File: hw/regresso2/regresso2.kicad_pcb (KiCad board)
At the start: 2 copper layers, 53.9 x 53.3 mm, 34 parts, among them J1 CONN_01X02, J2 Conn_01x08, J3 Conn_01x06, J4 Conn_01x10, J5 Conn_01x08, P10 CONTROL, P11 CONN_01X06, P9 FX2LA, U1 STM32L151C6TxA, U2 MIC550x-3.3YM5, Y1 Crystal_GND24_Small

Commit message: h2/regresso2: nearly "finished"
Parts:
- moved PB10 38.8 mm to (126.7, 105.4)
- moved PB11 38.8 mm to (126.7, 102.1)
- moved PB0 34.4 mm to (132.8, 114.4)
- moved PB1 32.7 mm to (134.0, 111.1)
- moved PA1 32.3 mm to (126.4, 110.4)
- moved PA0 31.2 mm to (128.0, 114.2)
- moved R1 22.9 mm to (135.6, 84.5), turned to 90 degrees
- moved JP1 18.9 mm to (133.1, 81.3), turned to 0 degrees
- moved R2 16.3 mm to (132.5, 86.2), turned to 180 degrees
- moved JP2 13.2 mm to (130.6, 81.3), turned to 0 degrees
- moved P11 2.84 mm to (152.3, 120.0)
- moved C4 1.39 mm to (145.0, 95.6)
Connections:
- J2 pad 1: (no net) -> Net-(J2-Pad1)
- J2 pad 2: (no net) -> Net-(J2-Pad2)
- J2 pad 3: (no net) -> Net-(J2-Pad3)
- J2 pad 4: (no net) -> Net-(J2-Pad4)
- J2 pad 5: (no net) -> Net-(J2-Pad5)
- J2 pad 8: (no net) -> Net-(J2-Pad8)
- J3 pad 4: (no net) -> Net-(J3-Pad4)
- J3 pad 5: (no net) -> Net-(J3-Pad5)
- J3 pad 6: (no net) -> Net-(J3-Pad6)
- J4 pad 2: (no net) -> Net-(J4-Pad2)
- J4 pad 3: (no net) -> Net-(J4-Pad3)
- J4 pad 8: (no net) -> Net-(J4-Pad8)
- J5 pad 1: (no net) -> Net-(J5-Pad1)
- J5 pad 2: (no net) -> Net-(J5-Pad2)
- J5 pad 4: (no net) -> Net-(J5-Pad4)
- J5 pad 5: (no net) -> Net-(J5-Pad5)
- J5 pad 6: (no net) -> Net-(J5-Pad6)
- J5 pad 7: (no net) -> Net-(J5-Pad7)
- J5 pad 8: (no net) -> /USART_CK_OUT
- P10 pad 4: (no net) -> Net-(P10-Pad4)
- P9 pad 3: /UART_TX_OUT -> /SPI_MOSI
- P9 pad 4: /UART_RX_OUT -> /SPI_MISO
- P9 pad 5: /SPI_MOSI -> /SPI_SCK
- P9 pad 6: /SPI_MISO -> /SPI_CS
- P9 pad 7: /SPI_SCK -> /UART_TX_OUT
- P9 pad 8: /SPI_CS -> /UART_RX_OUT
- P9 pad 9: (no net) -> Net-(P9-Pad9)
- R3 pad 1: (no net) -> /LED_CONTROL
- U1 pad 10: Net-(PA0-Pad1) -> Net-(U1-Pad10)
- U1 pad 11: Net-(PA1-Pad1) -> Net-(U1-Pad11)
- U1 pad 12: (no net) -> Net-(U1-Pad12)
- U1 pad 13: (no net) -> Net-(U1-Pad13)
- U1 pad 16: (no net) -> Net-(U1-Pad16)
- U1 pad 17: (no net) -> Net-(U1-Pad17)
- U1 pad 18: Net-(PB0-Pad1) -> Net-(U1-Pad18)
- U1 pad 19: Net-(PB1-Pad1) -> Net-(U1-Pad19)
- U1 pad 2: (no net) -> Net-(U1-Pad2)
- U1 pad 20: (no net) -> Net-(U1-Pad20)
- U1 pad 21: Net-(PB10-Pad1) -> Net-(U1-Pad21)
- U1 pad 22: Net-(PB11-Pad1) -> Net-(U1-Pad22)
- U1 pad 29: (no net) -> /UART_CK_OUT
- U1 pad 3: (no net) -> Net-(U1-Pad3)
- U1 pad 38: (no net) -> Net-(U1-Pad38)
- U1 pad 4: (no net) -> Net-(U1-Pad4)
- U1 pad 40: (no net) -> Net-(U1-Pad40)
- U1 pad 41: (no net) -> Net-(U1-Pad41)
- U1 pad 42: (no net) -> Net-(U1-Pad42)
- U1 pad 43: (no net) -> Net-(U1-Pad43)
- U2 pad 4: (no net) -> Net-(U2-Pad4)
- Y1 pad 2: (no net) -> Net-(Y1-Pad2)
- Y1 pad 4: (no net) -> Net-(Y1-Pad4)
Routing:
- net /SWDIO: track 8.93 -> 57.1 mm
- net +3V3: track 133.6 -> 88.8 mm, vias 6 -> 5
- net /UART_RX_OUT: track 32.7 -> 74.9 mm, vias 2 -> 0
- net /I2C_SDA: track 29.7 -> 61.8 mm
- net /SWCLK: track 11.1 -> 42.1 mm
- net Net-(U1-Pad16): track 28.2 -> 0.00 mm
- net /I2C_SCL: track 41.8 -> 67.4 mm
- net /SPI_CS: track 36.8 -> 57.2 mm, vias 1 -> 0
- net /SWO: track 9.32 -> 28.5 mm
- net /UART_TX_OUT: track 32.2 -> 50.6 mm, vias 2 -> 1
- net /NRST: track 9.68 -> 27.1 mm
- net Net-(PB11-Pad1): track 15.4 -> 0.00 mm
- net Net-(PB10-Pad1): track 12.8 -> 0.00 mm
- net Net-(PB1-Pad1): track 9.44 -> 0.00 mm
- net Net-(PA0-Pad1): track 8.31 -> 0.00 mm
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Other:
- board text removed: "ADC1-IN"

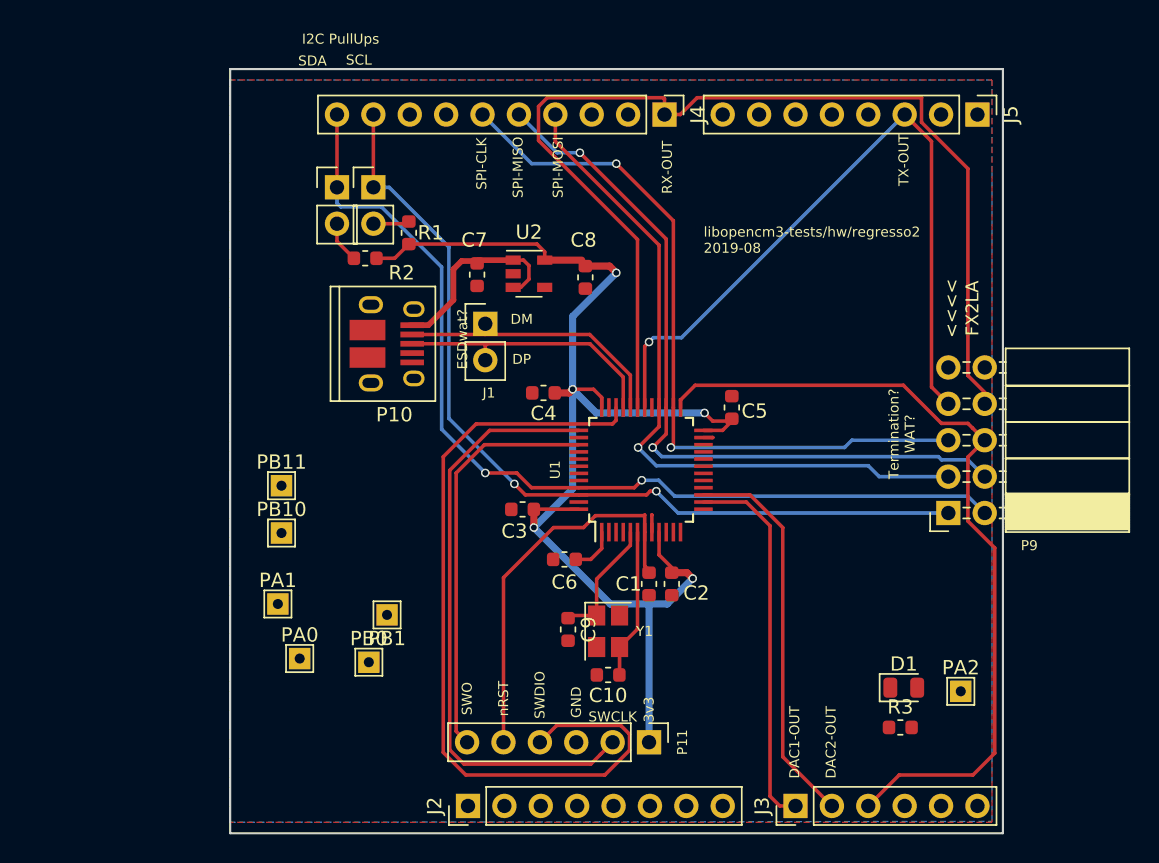
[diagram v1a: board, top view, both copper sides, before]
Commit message: hw/regresso2: "finished"
just need to start hacking at the board outline to fit around the nucleo
again.
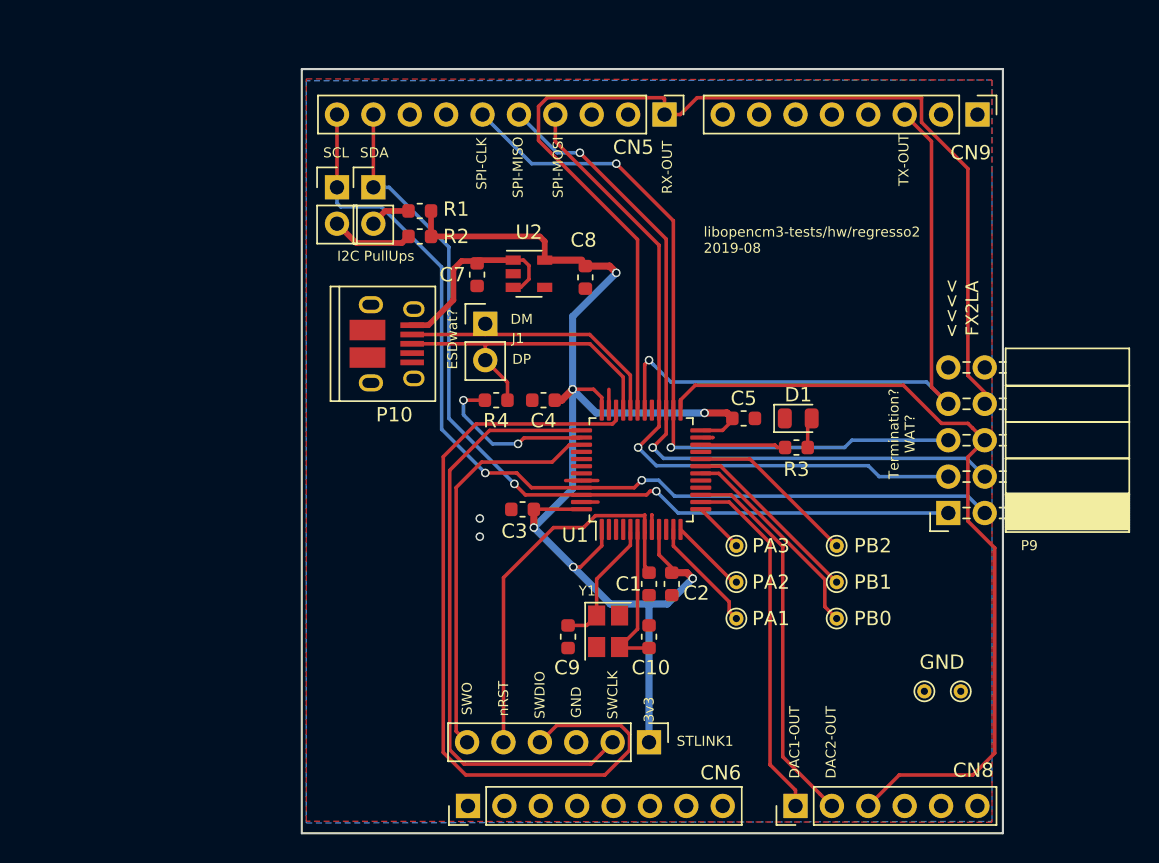
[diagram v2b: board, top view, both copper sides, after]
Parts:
- removed C6: 100n, Capacitor_SMD:C_0603_1608Metric
- removed PB11: TEST_1P, TestPoint:TestPoint_THTPad_1.5x1.5mm_Drill0.7mm
- added GND2: TEST_1P, TestPoint:TestPoint_THTPad_D1.0mm_Drill0.5mm, F.Cu at (171.6, 116.5)
- added PA1: TEST_1P, TestPoint:TestPoint_THTPad_D1.0mm_Drill0.5mm, F.Cu at (158.4, 111.4)
- added R4: 1,5k, Resistor_SMD:R_0603_1608Metric, F.Cu at (141.7, 96.1)
- GND1: renamed from PA2; footprint TestPoint:TestPoint_THTPad_1.5x1.5mm_Drill0.7mm -> TestPoint:TestPoint_THTPad_D1.0mm_Drill0.5mm
- PA2: renamed from PA0; footprint TestPoint:TestPoint_THTPad_1.5x1.5mm_Drill0.7mm -> TestPoint:TestPoint_THTPad_D1.0mm_Drill0.5mm
- PA3: renamed from PA1; footprint TestPoint:TestPoint_THTPad_1.5x1.5mm_Drill0.7mm -> TestPoint:TestPoint_THTPad_D1.0mm_Drill0.5mm
- PB0, PB1: footprint TestPoint:TestPoint_THTPad_1.5x1.5mm_Drill0.7mm -> TestPoint:TestPoint_THTPad_D1.0mm_Drill0.5mm
- PB2: renamed from PB10; footprint TestPoint:TestPoint_THTPad_1.5x1.5mm_Drill0.7mm -> TestPoint:TestPoint_THTPad_D1.0mm_Drill0.5mm
- STLINK1: renamed from P11; value CONN_01X06 -> STLINK
- U1: value STM32L151C6TxA -> STM32F303CCTx; footprint Housings_QFP:TQFP-48_7x7mm_Pitch0.5mm -> Package_QFP:LQFP-48_7x7mm_P0.5mm
- moved PB2 38.8 mm to (165.4, 106.3)
- moved PB0 32.8 mm to (165.4, 111.4)
- moved PA3 32.3 mm to (158.4, 106.3)
- moved PB1 31.5 mm to (165.4, 108.8)
- moved PA2 30.9 mm to (158.4, 108.8)
- moved R3 20.8 mm to (162.6, 99.4)
- moved D1 20.2 mm to (162.8, 97.4)
- moved R2 4.10 mm to (136.3, 84.7)
- moved C10 3.91 mm to (152.3, 112.6), turned to 90 degrees
- moved R1 1.70 mm to (136.3, 82.9), turned to 180 degrees
- moved C5 1.12 mm to (158.9, 97.4), turned to 0 degrees
- moved C4 0.51 mm to (145.0, 96.1)
- moved C9 0.51 mm to (146.7, 112.6)
- renumbered J4 to CN5, J2 to CN6, J3 to CN8, J5 to CN9
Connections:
- CN5 pad 2: Net-(J4-Pad2) -> (no net)
- CN5 pad 3: Net-(J4-Pad3) -> (no net)
- CN5 pad 8: Net-(J4-Pad8) -> (no net)
- CN6 pad 1: Net-(J2-Pad1) -> (no net)
- CN6 pad 2: Net-(J2-Pad2) -> (no net)
- CN6 pad 3: Net-(J2-Pad3) -> (no net)
- CN6 pad 4: Net-(J2-Pad4) -> (no net)
- CN6 pad 5: Net-(J2-Pad5) -> (no net)
- CN6 pad 8: Net-(J2-Pad8) -> (no net)
- CN8 pad 4: Net-(J3-Pad4) -> (no net)
- CN8 pad 5: Net-(J3-Pad5) -> (no net)
- CN8 pad 6: Net-(J3-Pad6) -> (no net)
- CN9 pad 1: Net-(J5-Pad1) -> (no net)
- CN9 pad 2: Net-(J5-Pad2) -> (no net)
- CN9 pad 4: Net-(J5-Pad4) -> (no net)
- CN9 pad 5: Net-(J5-Pad5) -> (no net)
- CN9 pad 6: Net-(J5-Pad6) -> (no net)
- CN9 pad 7: Net-(J5-Pad7) -> (no net)
- CN9 pad 8: /USART_CK_OUT -> (no net)
- P10 pad 4: Net-(P10-Pad4) -> (no net)
- P9 pad 9: Net-(P9-Pad9) -> (no net)
- PB2 pad 1: Net-(PB10-Pad1) -> Net-(PB2-Pad1)
- R3 pad 1: /LED_CONTROL -> /LED
- U1 pad 1: /VLCD -> +3V3
- U1 pad 10: Net-(U1-Pad10) -> (no net)
- U1 pad 12: Net-(U1-Pad12) -> Net-(PA0-Pad1)
- U1 pad 13: Net-(U1-Pad13) -> Net-(PA1-Pad1)
- U1 pad 16: Net-(U1-Pad16) -> (no net)
- U1 pad 17: Net-(U1-Pad17) -> (no net)
- U1 pad 18: Net-(U1-Pad18) -> Net-(PB0-Pad1)
- U1 pad 19: Net-(U1-Pad19) -> Net-(PB1-Pad1)
- U1 pad 2: Net-(U1-Pad2) -> (no net)
- U1 pad 20: Net-(U1-Pad20) -> Net-(PB2-Pad1)
- U1 pad 21: Net-(U1-Pad21) -> (no net)
- U1 pad 22: Net-(U1-Pad22) -> /LED
- U1 pad 29: /UART_CK_OUT -> (no net)
- U1 pad 3: Net-(U1-Pad3) -> (no net)
- U1 pad 4: Net-(U1-Pad4) -> (no net)
- U1 pad 40: Net-(U1-Pad40) -> (no net)
- U1 pad 41: Net-(U1-Pad41) -> (no net)
- U1 pad 42: Net-(U1-Pad42) -> (no net)
- U1 pad 43: Net-(U1-Pad43) -> (no net)
- U2 pad 4: Net-(U2-Pad4) -> (no net)
- Y1 pad 2: Net-(Y1-Pad2) -> (no net)
- Y1 pad 4: Net-(Y1-Pad4) -> (no net)
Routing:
- net Net-(PB0-Pad1): track 0.00 -> 14.8 mm
- net Net-(PB1-Pad1): track 0.00 -> 12.8 mm
- net Net-(PB2-Pad1): track 0.00 -> 12.0 mm
- net Net-(R4-Pad2): track 0.00 -> 11.8 mm, vias 0 -> 2
- net Net-(PB11-Pad1): track 0.00 -> 8.04 mm
- net /LED: track 0.00 -> 5.97 mm
- net Net-(PA0-Pad1): track 0.00 -> 5.42 mm
- net GND: track 1.87 -> 6.72 mm, vias 0 -> 2
- net Net-(PA1-Pad1): track 0.00 -> 3.58 mm
- net /UART_TX_OUT: track 50.6 -> 47.0 mm
- net /USB_DP: track 19.0 -> 22.4 mm
- net /VLCD: track 3.11 -> 0.00 mm
- net Net-(JP2-Pad2): track 2.90 -> 5.74 mm
- net Net-(D1-Pad2): track 0.00 -> 2.15 mm
- net +3V3: track 88.8 -> 90.9 mm, vias 5 -> 6
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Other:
- board size 53.9 x 53.3 mm -> 48.9 x 53.3 mm

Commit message: regresso2: board fixed
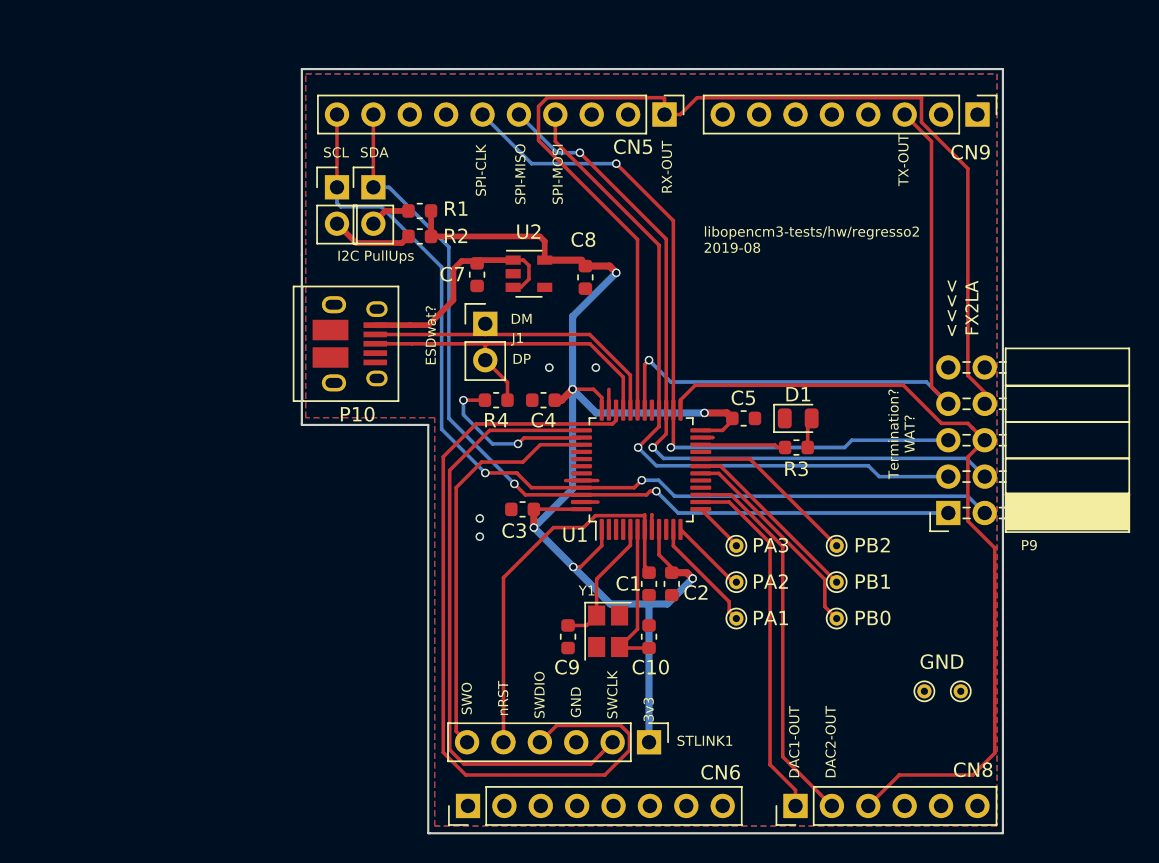
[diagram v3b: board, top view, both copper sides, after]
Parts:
- moved P10 2.58 mm to (131.7, 92.2)
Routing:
- net /USB_DM: track 18.7 -> 22.0 mm
- net /USB_DP: track 22.4 -> 25.0 mm
- net +5V: track 14.1 -> 16.5 mm
- net GND: vias 2 -> 4
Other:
- outline, holes or cut-outs redrawn
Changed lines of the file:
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@@
   (general
     (thickness 1.6)
-    (drawings 27)
-    (tracks 275)
+    (drawings 33)
+    (tracks 282)
     (modules 35)
     (nets 34)
@@
     (aux_axis_origin 123.1265 126.365)
     (grid_origin 123.1265 126.365)
-    (visible_elements FFFEFFFF)
+    (visible_elements FFFEF7FF)
     (pcbplotparams
       (layerselection 0x010f0_80000001)
@@
   )
   (module "Connectors:USB_Micro-B_10103594-0001LF" (layer "F.Cu")
-    (at 134.3025 92.202 270)
+    (at 131.7265 92.202 270)
     (descr "Micro USB Type B 10103594-0001LF")
     (tags "USB USB_B USB_micro USB_OTG")
@@
       (net 13 "Net-(P10-Pad6)"))
   )
+  (gr_line (start 128.1 97.765) (end 128.1 97.865) (layer "Edge.Cuts") (width 0.15))
+  (gr_line (start 130.7265 97.865) (end 128.1 97.865) (layer "Edge.Cuts") (width 0.15))
+  (gr_line (start 128.1 86) (end 128.1 97.765) (layer "Edge.Cuts") (width 0.15))
+  (gr_line (start 136.9265 126.365) (end 137.0457 126.365) (layer "Edge.Cuts") (width 0.15))
+  (gr_line (start 136.9265 97.865) (end 136.9265 126.365) (layer "Edge.Cuts") (width 0.15))
+  (gr_line (start 130.7265 97.865) (end 136.9265 97.865) (layer "Edge.Cuts") (width 0.15))
+  (gr_line (start 137.0457 126.365) (end 177.038 126.365) (angle 90) (layer "Edge.Cuts") (width 0.15))
   (gr_text "GND" (at 172.7835 114.427) (layer "F.SilkS")
     (effects (font (size 1 1) (thickness 0.15)))
@@
     (effects (font (size 0.7 0.7) (thickness 0.12)))
   )
-  (gr_text "SPI-CLK" (at 140.6525 79.629 90) (layer "F.SilkS")
+  (gr_text "SPI-CLK" (at 140.6265 80.115 90) (layer "F.SilkS")
     (effects (font (size 0.7 0.7) (thickness 0.12)))
   )
-  (gr_text "SPI-MISO" (at 143.1925 79.883 90) (layer "F.SilkS")
+  (gr_text "SPI-MISO" (at 143.3765 80.365 90) (layer "F.SilkS")
     (effects (font (size 0.7 0.7) (thickness 0.12)))
   )
-  (gr_text "SPI-MOSI" (at 145.9865 79.883 90) (layer "F.SilkS")
+  (gr_text "SPI-MOSI" (at 145.9865 80.365 90) (layer "F.SilkS")
     (effects (font (size 0.7 0.7) (thickness 0.12)))
   )
@@
     (effects (font (size 0.7 0.7) (thickness 0.12)))
   )
-  (gr_text "ESDwat?" (at 138.6205 91.8845 90) (layer "F.SilkS")
+  (gr_text "ESDwat?" (at 137.1265 91.615 90) (layer "F.SilkS")
     (effects (font (size 0.7 0.7) (thickness 0.12)))
   )
   (gr_line (start 177.038 126.365) (end 177.038 73.025) (angle 90) (layer "Edge.Cuts") (width 0.15))
-  (gr_line (start 128.1 126.365) (end 177.038 126.365) (angle 90) (layer "Edge.Cuts") (width 0.15))
-  (gr_line (start 128.1 73.025) (end 128.1 126.365) (angle 90) (layer "Edge.Cuts") (width 0.15))
+  (gr_line (start 128.1 73.025) (end 128.1 86) (angle 90) (layer "Edge.Cuts") (width 0.15))
   (gr_line (start 177.038 73.025) (end 128.1 73.025) (angle 90) (layer "Edge.Cuts") (width 0.15))
+  (via (at 148.6265 93.865) (size 0.6) (drill 0.4) (layers "F.Cu" "B.Cu") (net 2))
+  (via (at 145.3765 93.865) (size 0.6) (drill 0.4) (layers "F.Cu" "B.Cu") (net 2))
+  (segment (start 143.5345 100.457) (end 144.7445 99.247) (width 0.25) (layer "F.Cu") (net 16))
+  (segment (start 144.7445 99.247) (end 146.785 99.247) (width 0.25) (layer "F.Cu") (net 16))
+  (segment (start 140.6525 100.457) (end 143.5345 100.457) (width 0.25) (layer "F.Cu") (net 16))
+  (segment (start 140.9135 91.552) (end 148.19682 91.552) (width 0.25) (layer "F.Cu") (net 11))
+  (segment (start 140.9065 91.545) (end 140.9135 91.552) (width 0.25) (layer "F.Cu") (net 11))
+  (segment (start 133.2265 91.552) (end 140.9135 91.552) (width 0.25) (layer "F.Cu") (net 11))
+  (segment (start 140.9065 90.805) (end 140.9065 91.545) (width 0.25) (layer "F.Cu") (net 11))
+  (segment (start 135.8025 92.202) (end 133.2265 92.202) (width 0.25) (layer "F.Cu") (net 12))
+  (segment (start 148.19682 91.552) (end 151.035 94.39018) (width 0.25) (layer "F.Cu") (net 11))
+  (segment (start 151.035 94.39018) (end 151.035 96.647) (width 0.25) (layer "F.Cu") (net 11))
+  (segment (start 135.6525 90.902) (end 133.2265 90.902) (width 0.4) (layer "F.Cu") (net 1))
   (segment (start 146.685 111.8615) (end 147.9855 111.8615) (width 0.25) (layer "F.Cu") (net 23))
   (segment (start 147.9855 111.8615) (end 148.679 111.168) (width 0.25) (layer "F.Cu") (net 23))
@@
   (segment (start 146.2405 96.139) (end 147.0025 95.377) (width 0.5) (layer "F.Cu") (net 3))
   (via (at 143.1925 99.187) (size 0.6) (drill 0.4) (layers "F.Cu" "B.Cu") (net 31))
-  (segment (start 146.785 99.247) (end 145.575 100.457) (width 0.25) (layer "F.Cu") (net 16))
   (segment (start 147.6225 99.247) (end 146.785 99.247) (width 0.25) (layer "F.Cu") (net 16))
   (segment (start 140.6525 100.457) (end 138.8745 102.235) (width 0.25) (layer "F.Cu") (net 16))
   (segment (start 138.8745 102.235) (end 138.8745 119.253) (width 0.25) (layer "F.Cu") (net 16))
-  (segment (start 145.575 100.457) (end 140.6525 100.457) (width 0.25) (layer "F.Cu") (net 16))
   (segment (start 138.8745 119.253) (end 139.6365 120.015) (width 0.25) (layer "F.Cu") (net 16))
   (segment (start 147.047 107.7785) (end 144.2975 105.029) (width 0.5) (layer "B.Cu") (net 3))
@@
   (segment (start 148.209315 92.200905) (end 150.535 94.52659) (width 0.25) (layer "F.Cu") (net 12))
   (segment (start 150.535 94.52659) (end 150.535 96.647) (width 0.25) (layer "F.Cu") (net 12))
-  (segment (start 151.035 96.647) (end 151.035 94.39018) (width 0.25) (layer "F.Cu") (net 11))
-  (segment (start 148.19682 91.552) (end 151.035 94.39018) (width 0.25) (layer "F.Cu") (net 11))
   (via (at 151.5745 99.441) (size 0.6) (drill 0.4) (layers "F.Cu" "B.Cu") (net 8))
   (segment (start 153.035 96.647) (end 153.035 97.9805) (width 0.25) (layer "F.Cu") (net 8))
@@
   (segment (start 153.6065 110.363) (end 152.3365 110.363) (width 0.5) (layer "B.Cu") (net 3))
   (segment (start 155.3845 108.585) (end 153.6065 110.363) (width 0.5) (layer "B.Cu") (net 3))
-  (segment (start 135.8025 91.552) (end 140.8915 91.552) (width 0.25) (layer "F.Cu") (net 11))
-  (segment (start 140.8915 91.552) (end 148.19682 91.552) (width 0.25) (layer "F.Cu") (net 11))
   (via (at 144.2975 105.029) (size 0.6) (drill 0.4) (layers "F.Cu" "B.Cu") (net 3))
   (segment (start 144.2975 103.759) (end 144.2975 105.029) (width 0.5) (layer "F.Cu") (net 3))
@@
   (segment (start 152.5905 99.441) (end 153.3525 100.203) (width 0.25) (layer "B.Cu") (net 9))
   (segment (start 153.3525 100.203) (end 174.498 100.203) (width 0.25) (layer "B.Cu") (net 9))
-  (zone (net 2) (net_name "GND") (layer "B.Cu") (hatch edge 0.508)
-    (connect_pads (clearance 0.508))
+  (zone (net 2) (net_name "GND") (layer "F.Cu") (hatch edge 0.508)
+    (connect_pads (clearance 0.25))
     (min_thickness 0.254)
     (fill yes (thermal_gap 0.508) (thermal_bridge_width 0.508))
     (polygon
       (pts
-        (xy 128.4097 73.840624) (xy 128.4097 125.650976) (xy 176.276 125.5395) (xy 176.276 80.2005) (xy 176.276 73.787)
+        (xy 176.6265 73.365) (xy 176.6265 125.865) (xy 137.3765 125.865) (xy 137.3765 97.365) (xy 128.3765 97.365)
+        (xy 128.3765 73.365)
       )
     )
   )
-  (zone (net 2) (net_name "GND") (layer "F.Cu") (hatch edge 0.508)
+  (zone (net 2) (net_name "GND") (layer "B.Cu") (hatch edge 0.508)
     (connect_pads (clearance 0.25))
-    (min_thickness 0.25)
-    (fill yes (thermal_gap 0.25) (thermal_bridge_width 0.3))
+    (min_thickness 0.254)
+    (fill yes (thermal_gap 0.508) (thermal_bridge_width 0.508))
     (polygon
       (pts
-        (xy 176.276 125.603) (xy 128.4097 125.5268) (xy 128.4097 73.7108) (xy 176.276 73.787)
+        (xy 176.6265 73.365) (xy 176.6265 125.865) (xy 137.3765 125.865) (xy 137.3765 97.365) (xy 128.3765 97.365)
+        (xy 128.3765 73.365)
       )
     )
